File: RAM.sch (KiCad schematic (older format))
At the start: 8 parts

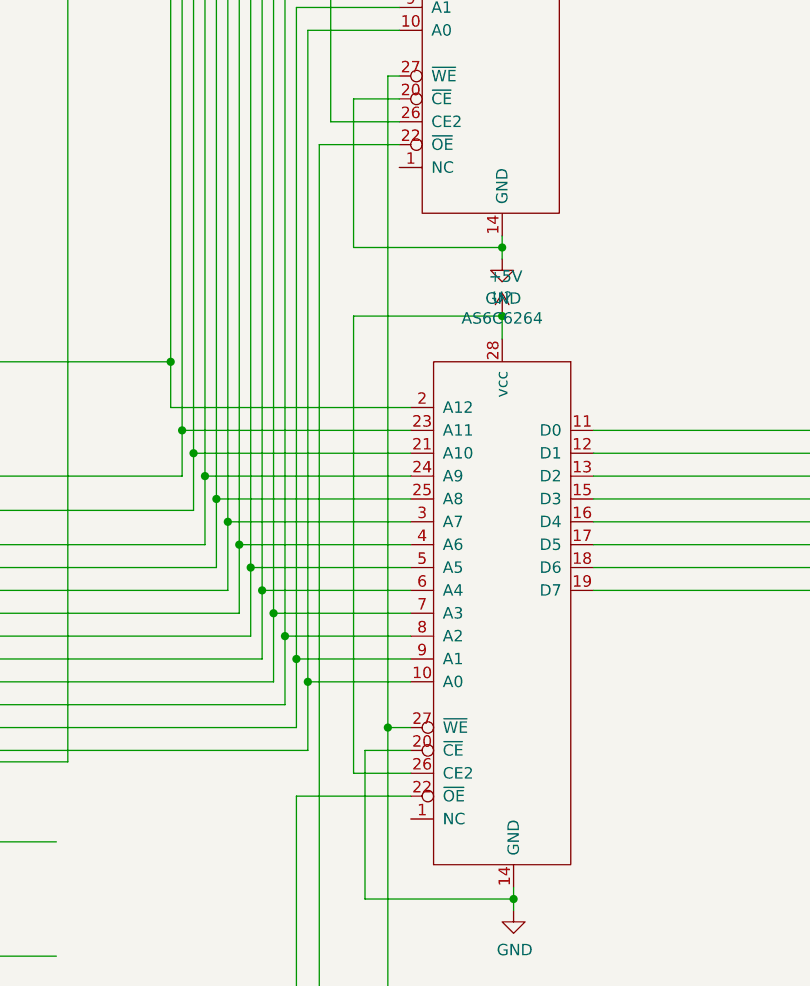
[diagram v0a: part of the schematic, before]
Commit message: ram connected,need to add and a cap
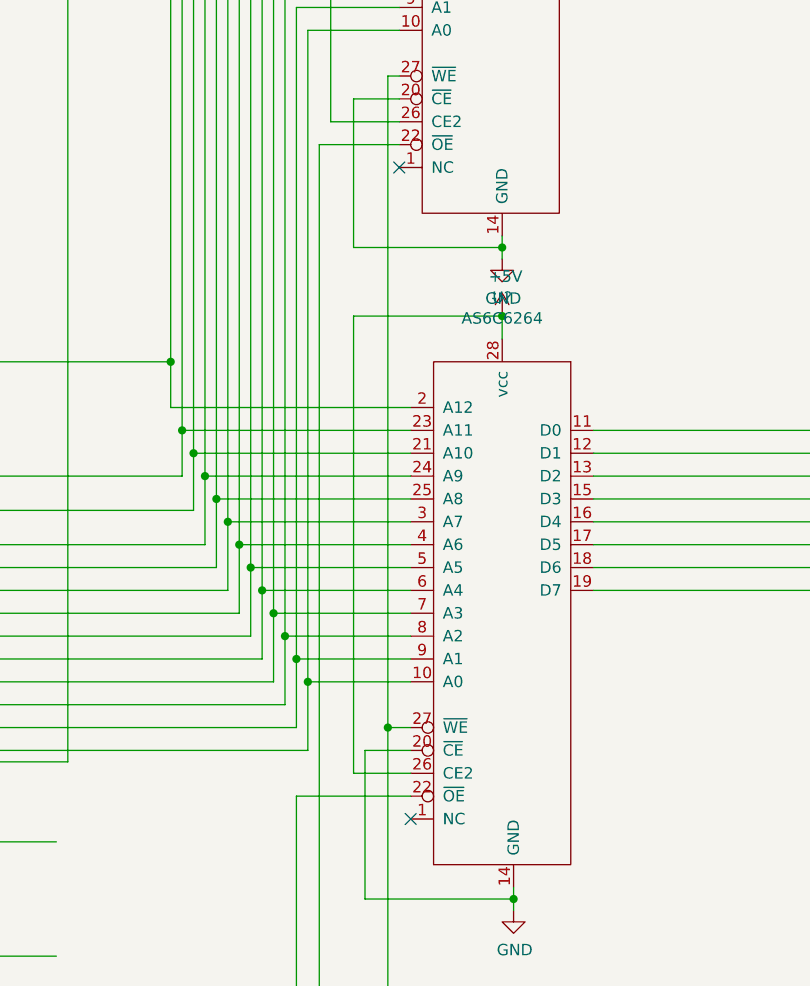
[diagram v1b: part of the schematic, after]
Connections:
- no-connect marks 0 -> 2
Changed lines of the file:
@@
 	12200 5550 12200 5600
 Connection ~ 12200 5550
+NoConn ~ 11800 8050
+NoConn ~ 11750 5200
 $EndSCHEMATC

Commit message: Added ROM with 2 inverter cap nonsense
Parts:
- added C?: 0.01uF, symbol Device:C
- added R?: 1K, symbol Device:R
- added U? (x2): AT28C64B-15PU, DIP1555W45P254L3733H482Q28, symbol AT28C64B-15PU:AT28C64B-15PU
- added U?: 74HC00, symbol 74xx:74HC00
- added U? (x2): 74AHC04, symbol 74xx:74AHC04
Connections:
- net labels added: MEMWE
- net labels removed: ~MEMWE
- wire segments 371 -> 506

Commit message: Added footprints
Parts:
- removed U? (x2): 74AHC04, symbol 74xx:74AHC04
- added U32: 74HC04, Package_DIP:DIP-14_W7.62mm, symbol 74xx:74HC04
- C6: renamed from C?; footprint (none) -> Capacitor_THT:CP_Axial_L10.0mm_D4.5mm_P15.00mm_Horizontal
- R7: renamed from R?; footprint (none) -> Resistor_THT:R_Axial_DIN0204_L3.6mm_D1.6mm_P7.62mm_Horizontal
- U34: renamed from U?; footprint (none) -> Package_DIP:DIP-14_W7.62mm
- U39, U40: renamed from U?; footprint (none) -> Package_DIP:DIP-28_W15.24mm
- U41, U42: renamed from U?; footprint DIP1555W45P254L3733H482Q28 -> ROM:3M_240-1280-00-0602J
- gave numbers to parts that had none: 6

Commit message: Added IR,Cu started
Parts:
- renumbered C6 to C?, R7 to R?, U39 to U?, U40 to U?, U41 to U?, U42 to U?, U34 to U?, U32 to U?
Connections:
- wire segments 506 -> 505
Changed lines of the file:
@@
 $Descr A2 23386 16535
 encoding utf-8
-Sheet 6 7
+Sheet 7 9
 Title ""
 Date ""
@@
 Wire Wire Line
 	4700 3050 4700 650
-Wire Wire Line
-	1350 650  1450 650
 Connection ~ 4700 650
 Wire Wire Line
@@
 Wire Wire Line
 	7150 4850 7150 5350
-Text HLabel 1350 650  0    50   Input ~ 0
-CLK
-Text HLabel 1350 900  0    50   3State ~ 0
-Bus0
-Text HLabel 1350 1000 0    50   3State ~ 0
-Bus1
-Text HLabel 1350 1100 0    50   3State ~ 0
-Bus2
-Text HLabel 1350 1200 0    50   3State ~ 0
-Bus3
-Text HLabel 1350 1300 0    50   3State ~ 0
-Bus4
-Text HLabel 1350 1400 0    50   3State ~ 0
-Bus5
-Text HLabel 1350 1500 0    50   3State ~ 0
-Bus6
-Text HLabel 1350 1600 0    50   3State ~ 0
-Bus7
-Text HLabel 1350 1700 0    50   3State ~ 0
-Bus8
-Text HLabel 1350 1800 0    50   3State ~ 0
-Bus9
-Text HLabel 1350 1900 0    50   3State ~ 0
-Bus10
-Text HLabel 1350 2000 0    50   3State ~ 0
-Bus11
-Text HLabel 1350 2100 0    50   3State ~ 0
-Bus12
-Text HLabel 1350 2200 0    50   3State ~ 0
-Bus13
-Text HLabel 1350 2300 0    50   3State ~ 0
-Bus14
-Text HLabel 1350 2400 0    50   3State ~ 0
-Bus15
 $Comp
 L 74xx:74LS173 U?
@@
 $EndComp
 $Comp
-L draguve:AS6C6264 U39
+L draguve:AS6C6264 U?
 U 1 1 5F6F3976
 P 11650 4500
-F 0 "U39" H 12150 6081 50  0000 C CNN
+F 0 "U?" H 12150 6081 50  0000 C CNN
 F 1 "AS6C6264" H 12150 5990 50  0000 C CNN
 F 2 "Package_DIP:DIP-28_W15.24mm" H 12300 6200 50  0001 C CNN
@@
 Connection ~ 11700 7650
 $Comp
-L power:+5V #PWR0108
+L power:+5V #PWR?
 U 1 1 60204631
 P 12150 3000
-F 0 "#PWR0108" H 12150 2850 50  0001 C CNN
+F 0 "#PWR?" H 12150 2850 50  0001 C CNN
 F 1 "+5V" H 12165 3173 50  0000 C CNN
 F 2 "" H 12150 3000 50  0001 C CNN
@@
 $EndComp
 $Comp
-L power:+5V #PWR0110
+L power:+5V #PWR?
 U 1 1 602074BD
 P 12200 5850
-F 0 "#PWR0110" H 12200 5700 50  0001 C CNN
+F 0 "#PWR?" H 12200 5700 50  0001 C CNN
 F 1 "+5V" H 12215 6023 50  0000 C CNN
 F 2 "" H 12200 5850 50  0001 C CNN
@@
 	12200 5500 12200 5550
 $Comp
-L power:GND #PWR0109
+L power:GND #PWR?
 U 1 1 6038BAE8
 P 12200 5600
-F 0 "#PWR0109" H 12200 5350 50  0001 C CNN
+F 0 "#PWR?" H 12200 5350 50  0001 C CNN
 F 1 "GND" H 12205 5427 50  0000 C CNN
 F 2 "" H 12200 5600 50  0001 C CNN
@@
 	12250 8350 12250 8400
 $Comp
-L power:GND #PWR0111
+L power:GND #PWR?
 U 1 1 603EEA99
 P 12250 8450
-F 0 "#PWR0111" H 12250 8200 50  0001 C CNN
+F 0 "#PWR?" H 12250 8200 50  0001 C CNN
 F 1 "GND" H 12255 8277 50  0000 C CNN
 F 2 "" H 12250 8450 50  0001 C CNN
@@
 NoConn ~ 11750 5200
 $Comp
-L AT28C64B-15PU:AT28C64B-15PU U41
+L AT28C64B-15PU:AT28C64B-15PU U?
 U 1 1 5F7A0947
 P 12700 10850
-F 0 "U41" H 12700 12020 50  0000 C CNN
+F 0 "U?" H 12700 12020 50  0000 C CNN
 F 1 "AT28C64B-15PU" H 12700 11929 50  0000 C CNN
 F 2 "ROM:3M_240-1280-00-0602J" H 12700 10850 50  0001 L BNN
@@
 $EndComp
 $Comp
-L AT28C64B-15PU:AT28C64B-15PU U42
+L AT28C64B-15PU:AT28C64B-15PU U?
 U 1 1 5F7AF1E8
 P 12700 13100
-F 0 "U42" H 12700 14270 50  0000 C CNN
+F 0 "U?" H 12700 14270 50  0000 C CNN
 F 1 "AT28C64B-15PU" H 12700 14179 50  0000 C CNN
 F 2 "ROM:3M_240-1280-00-0602J" H 12700 13100 50  0001 L BNN
@@
 $EndComp
 Connection ~ 11300 9250
-Text HLabel 1300 9500 0    50   Input ~ 0
-MEMWE
 Wire Wire Line
 	1300 9250 8650 9250
-Text HLabel 1300 9250 0    50   Input ~ 0
-~MEMOE
-Text HLabel 1400 7800 0    50   Input ~ 0
-CLR
-Text HLabel 1450 8150 0    50   Input ~ 0
-~AI
 Wire Wire Line
 	4750 3950 4750 8150
 Wire Wire Line
 	10300 3100 10300 7800
-Text HLabel 1400 7800 0    50   Input ~ 0
-CLR
-Text HLabel 1400 8650 0    50   Input ~ 0
-~AO
 Wire Wire Line
 	6550 8650 10250 8650
@@
 Wire Wire Line
 	6550 5350 6550 8650
-Connection ~ 4750 8150
-Wire Wire Line
-	1450 8150 4750 8150
 Wire Wire Line
 	1500 8650 6550 8650
@@
 	17550 1600 22700 1600
 $Comp
-L power:+5V #PWR0112
+L power:+5V #PWR?
 U 1 1 605F9C09
 P 13400 9950
-F 0 "#PWR0112" H 13400 9800 50  0001 C CNN
+F 0 "#PWR?" H 13400 9800 50  0001 C CNN
 F 1 "+5V" H 13415 10123 50  0000 C CNN
 F 2 "" H 13400 9950 50  0001 C CNN
@@
 $EndComp
 $Comp
-L power:+5V #PWR0114
+L power:+5V #PWR?
 U 1 1 60630E61
 P 13400 12200
-F 0 "#PWR0114" H 13400 12050 50  0001 C CNN
+F 0 "#PWR?" H 13400 12050 50  0001 C CNN
 F 1 "+5V" H 13415 12373 50  0000 C CNN
 F 2 "" H 13400 12200 50  0001 C CNN
@@
 $EndComp
 $Comp
-L power:GND #PWR0113
+L power:GND #PWR?
 U 1 1 6066970A
 P 13400 11750
-F 0 "#PWR0113" H 13400 11500 50  0001 C CNN
+F 0 "#PWR?" H 13400 11500 50  0001 C CNN
 F 1 "GND" H 13405 11577 50  0000 C CNN
 F 2 "" H 13400 11750 50  0001 C CNN
@@
 $EndComp
 $Comp
-L power:GND #PWR0115
+L power:GND #PWR?
 U 1 1 606A094E
 P 13400 14000
-F 0 "#PWR0115" H 13400 13750 50  0001 C CNN
+F 0 "#PWR?" H 13400 13750 50  0001 C CNN
 F 1 "GND" H 13405 13827 50  0000 C CNN
 F 2 "" H 13400 14000 50  0001 C CNN
@@
 	9300 7850 11800 7850
 $Comp
-L draguve:AS6C6264 U40
+L draguve:AS6C6264 U?
 U 1 1 5F715537
 P 11700 7350
-F 0 "U40" H 12200 8931 50  0000 C CNN
+F 0 "U?" H 12200 8931 50  0000 C CNN
 F 1 "AS6C6264" H 12200 8840 50  0000 C CNN
 F 2 "Package_DIP:DIP-28_W15.24mm" H 12350 9050 50  0001 C CNN
@@
 	12150 3000 12150 3100
 $Comp
-L power:GND #PWR0106
+L power:GND #PWR?
 U 1 1 60A67B07
 P 12000 10250
-F 0 "#PWR0106" H 12000 10000 50  0001 C CNN
+F 0 "#PWR?" H 12000 10000 50  0001 C CNN
 F 1 "GND" H 12005 10077 50  0000 C CNN
 F 2 "" H 12000 10250 50  0001 C CNN
@@
 $EndComp
 $Comp
-L power:GND #PWR0107
+L power:GND #PWR?
 U 1 1 60AA17EB
 P 12000 12500
-F 0 "#PWR0107" H 12000 12250 50  0001 C CNN
+F 0 "#PWR?" H 12000 12250 50  0001 C CNN
 F 1 "GND" H 12005 12327 50  0000 C CNN
 F 2 "" H 12000 12500 50  0001 C CNN
@@
 $EndComp
 $Comp
-L 74xx:74HC00 U34
+L 74xx:74HC00 U?
 U 1 1 60C0C0E9
 P 4750 10450
-F 0 "U34" H 4750 10775 50  0000 C CNN
+F 0 "U?" H 4750 10775 50  0000 C CNN
 F 1 "74HC00" H 4750 10684 50  0000 C CNN
 F 2 "Package_DIP:DIP-14_W7.62mm" H 4750 10450 50  0001 C CNN
@@
 	1    0    0    -1
 $EndComp
-Wire Wire Line
-	1450 650  1450 8150
-Wire Wire Line
-	1450 10250 2550 10250
-Connection ~ 1450 650
-Wire Wire Line
-	1450 650  3150 650
-Connection ~ 1450 8150
-Wire Wire Line
-	1450 8150 1450 10250
-$Comp
-L Device:C C6
+$Comp
+L Device:C C?
 U 1 1 60C529CD
 P 3750 10400
-F 0 "C6" H 3865 10446 50  0000 L CNN
+F 0 "C?" H 3865 10446 50  0000 L CNN
 F 1 "0.01uF" H 3865 10355 50  0000 L CNN
 F 2 "Capacitor_THT:CP_Axial_L10.0mm_D4.5mm_P15.00mm_Horizontal" H 3788 10250 50  0001 C CNN
@@
 	4350 10550 4450 10550
 $Comp
-L power:GND #PWR087
+L power:GND #PWR?
 U 1 1 60E7A445
 P 4350 11150
-F 0 "#PWR087" H 4350 10900 50  0001 C CNN
+F 0 "#PWR?" H 4350 10900 50  0001 C CNN
 F 1 "GND" H 4355 10977 50  0000 C CNN
 F 2 "" H 4350 11150 50  0001 C CNN
@@
 $EndComp
 $Comp
-L Device:R R7
+L Device:R R?
 U 1 1 60EBB69C
 P 4350 11000
-F 0 "R7" H 4420 11046 50  0000 L CNN
+F 0 "R?" H 4420 11046 50  0000 L CNN
 F 1 "1K" H 4420 10955 50  0000 L CNN
 F 2 "Resistor_THT:R_Axial_DIN0204_L3.6mm_D1.6mm_P7.62mm_Horizontal" V 4280 11000 50  0001 C CNN
@@
 	4200 9500 15750 9500
 $Comp
-L 74xx:74HC04 U32
+L 74xx:74HC04 U?
 U 1 1 6116F1B1
 P 2850 10250
-F 0 "U32" H 2850 10567 50  0000 C CNN
+F 0 "U?" H 2850 10567 50  0000 C CNN
 F 1 "74HC04" H 2850 10476 50  0000 C CNN
 F 2 "Package_DIP:DIP-14_W7.62mm" H 2850 10250 50  0001 C CNN
@@
 $EndComp
 $Comp
-L 74xx:74HC04 U32
+L 74xx:74HC04 U?
 U 2 1 61170EAC
 P 3450 10250
-F 0 "U32" H 3450 10567 50  0000 C CNN
+F 0 "U?" H 3450 10567 50  0000 C CNN
 F 1 "74HC04" H 3450 10476 50  0000 C CNN
 F 2 "Package_DIP:DIP-14_W7.62mm" H 3450 10250 50  0001 C CNN
@@
 	1    0    0    -1
 $EndComp
+Text HLabel 1450 8150 0    50   Input ~ 0
+~AI
+Connection ~ 4750 8150
+Wire Wire Line
+	1450 8150 4750 8150
+Wire Wire Line
+	1700 650  1700 10250
+Connection ~ 1700 650
+Wire Wire Line
+	1700 650  3150 650
+Wire Wire Line
+	1700 10250 2550 10250
+Wire Wire Line
+	1350 650  1700 650
+Text HLabel 1300 9250 0    50   Input ~ 0
+~MEMOE
+Text HLabel 1300 9500 0    50   Input ~ 0
+MEMWE
+Text HLabel 1400 8650 0    50   Input ~ 0
+~AO
+Text HLabel 1400 7800 0    50   Input ~ 0
+CLR
 $EndSCHEMATC

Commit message: Fixed power for multi part comps
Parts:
- added unit 5 of U35
- added unit 7 of U37
- gave numbers to parts that had none: 8
- renumbered U31 to U36, U33 to U38, U35 to U39, U36 to U40, U37 to U41, U38 to U42
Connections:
- wire segments 505 -> 507

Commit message: Fixed ZIF
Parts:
- C6: symbol Device:C -> 16bitCpu-rescue:C-Device
- R7: symbol Device:R -> 16bitCpu-rescue:R-Device
- U35: symbol 74xx:74HC00 -> 16bitCpu-rescue:74HC00-74xx
- U36, U40: symbol 74xx:74LS245 -> 16bitCpu-rescue:74LS245-74xx
- U37: symbol 74xx:74HC04 -> 16bitCpu-rescue:74HC04-74xx
- U38, U39, U41, U42: symbol 74xx:74LS173 -> 16bitCpu-rescue:74LS173-74xx
- U45, U46: footprint ROM:3M_240-1280-00-0602J -> ROM:ZIF-AT28C64B-15PU

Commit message: changed ir to only hold 12
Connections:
- net labels added: GND-power
- wire segments 507 -> 509
- no-connect marks 2 -> 5
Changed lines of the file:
@@
 	8800 650  15800 650
 Wire Wire Line
-	9200 6050 10750 6050
-Wire Wire Line
-	10750 6050 10750 3400
-Wire Wire Line
-	10750 3400 11750 3400
-Wire Wire Line
-	10750 6050 10750 6250
+	10750 3400 10950 3400
 Wire Wire Line
 	10750 6250 11800 6250
-Connection ~ 10750 6050
 Wire Wire Line
 	10800 3500 11750 3500
@@
 	1    0    0    -1
 $EndComp
+Wire Wire Line
+	10750 3400 10750 6250
+NoConn ~ 9200 6050
+Wire Wire Line
+	10950 3400 10950 2700
+Wire Wire Line
+	10950 2700 11350 2700
+Wire Wire Line
+	11350 2700 11350 3000
+Connection ~ 10950 3400
+Wire Wire Line
+	10950 3400 11750 3400
+$Comp
+L 16bitCpu-rescue:GND-power #PWR?
+U 1 1 5FAE8C08
+P 11350 3000
+F 0 "#PWR?" H 11350 2750 50  0001 C CNN
+F 1 "GND-power" H 11355 2827 50  0000 C CNN
+F 2 "" H 11350 3000 50  0001 C CNN
+F 3 "" H 11350 3000 50  0001 C CNN
+	1    11350 3000
+	1    0    0    -1
+$EndComp
+NoConn ~ 10250 8150
+NoConn ~ 10250 8650
 $EndSCHEMATC
